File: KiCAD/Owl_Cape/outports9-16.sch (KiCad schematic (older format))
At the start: 33 parts, among them IC2 SN74LVC245AN, J10 G D V, J11 G D V, J12 G D V, J13 G D V, J14 G D V, J15 G D V, J16 G D V, J17 G D V

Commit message: updates to power components
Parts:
- renumbered J10 to J11, J11 to J12, J12 to J13, J13 to J14, J14 to J15, J15 to J16, J16 to J17, J17 to J18, R9 to R17, R10 to R18, R11 to R19, R12 to R20, R13 to R21, R14 to R22, R15 to R23, R16 to R24

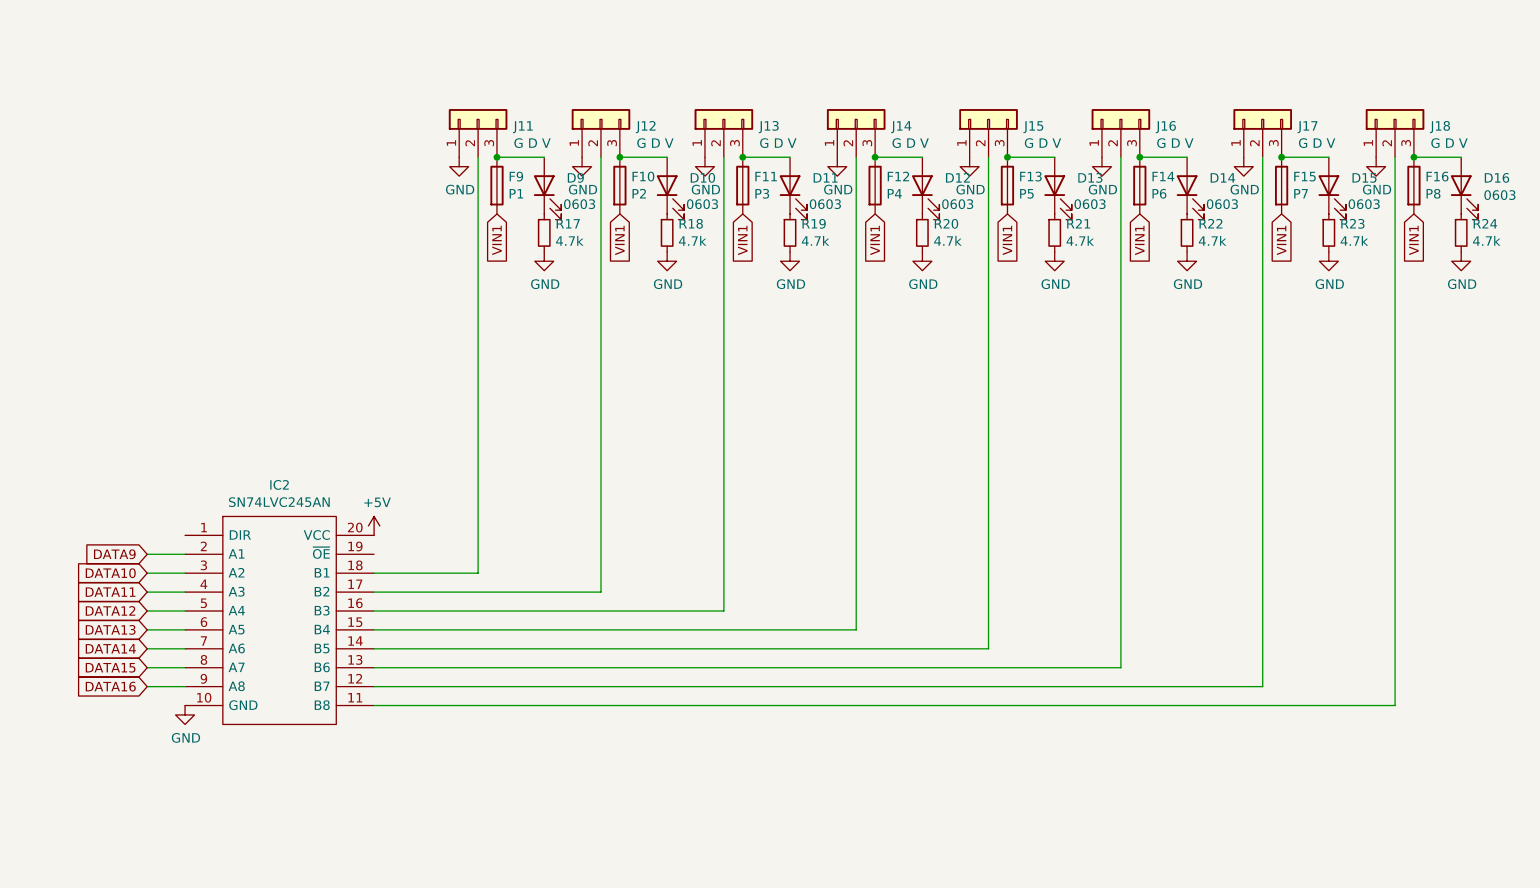
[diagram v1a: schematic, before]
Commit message: logo and kicad updates
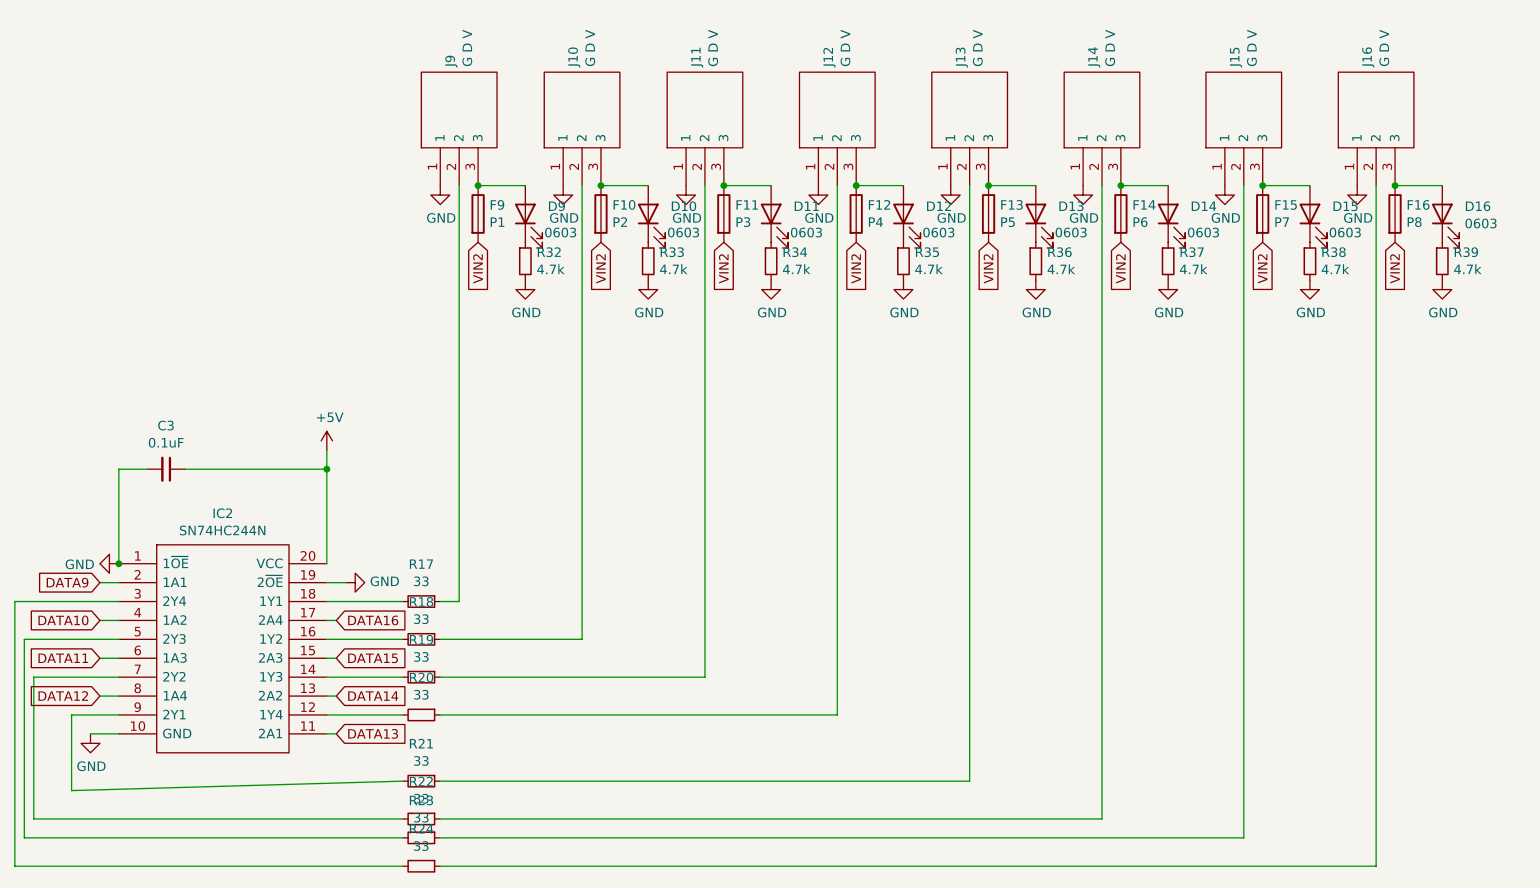
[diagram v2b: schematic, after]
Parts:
- removed IC2: SN74LVC245AN, SamacSys_Parts:DIP794W53P254L2540H508Q20N, symbol SamacSys_Parts:SN74LVC245AN
- removed J11, J12, J13, J14, J15, J16, J17, J18: G D V, PhoenixContact_MCV_1,5_3-G-3.5_1x03_P3.50mm_Vertical_Tim, symbol Connector_Generic:Conn_01x03
- added C3: 0.1uF, Capacitor_SMD:CP_Elec_4x5.3, symbol Device:C_Small
- added IC2: SN74HC244N, SamacSys_Parts:DIP794W53P254L2540H508Q20N, symbol SamacSys_Parts:SN74HC244N
- added J10, J11, J12, J13, J14, J15, J16, J9: G D V, SamacSys_Parts:SHDR3W80P0X350_1X3_1250X725X940P, symbol SamacSys_Parts:284514-3
- added R32, R33, R34, R35, R36, R37, R38, R39: 4.7k, Resistor_SMD:R_0805_2012Metric, symbol Device:R_Small
- D10, D11, D12, D13, D14, D15, D16, D9: footprint 3544again:LED_0603_1608Metric -> LED_SMD:LED_0603_1608Metric
- F10, F11, F12, F13, F14, F15, F16, F9: footprint 3544again:3544-2 -> Fuse:Fuseholder_Blade_Mini_Keystone_3568
- R17, R18, R19, R20, R21, R22, R23, R24: value 4.7k -> 33; footprint 3544again:R_0805_2012Metric -> Resistor_SMD:R_0805_2012Metric; Description C17673 -> (none)
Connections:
- net +5V: now also C3.1, IC2.20 (VCC)
- net DATA10: now also IC2.4 (1A2)
- net DATA11: now also IC2.6 (1A3)
- net DATA12: now also IC2.8 (1A4)
- net DATA13: now also IC2.11 (2A1)
- net DATA14: now also IC2.13 (2A2)
- net DATA15: now also IC2.15 (2A3)
- net DATA16: now also IC2.17 (2A4)
- net DATA9: now also IC2.2 (1A1)
- net GND: now also C3.2, IC2.1 (1~OE), IC2.10 (GND), IC2.19 (2~OE), J10.1, J11.1, J12.1, J13.1, J14.1, J15.1, J16.1, J9.1, R32.2, R33.2, R34.2, R35.2, R36.2, R37.2, R38.2, R39.2; no longer R17.2, R18.2, R19.2, R20.2, R21.2, R22.2, R23.2, R24.2
- net at D9.2 (A), F9.1: now also J9.3
- net at D10.2 (A), F10.1: now also J10.3
- net at D11.2 (A), F11.1: now also J11.3
- net at D12.2 (A), F12.1: now also J12.3
- net at D13.2 (A), F13.1: now also J13.3
- net at D14.2 (A), F14.1: now also J14.3
- net at D15.2 (A), F15.1: now also J15.3
- net at D16.2 (A), F16.1: now also J16.3
- net at D16.1 (K): now also R39.1; no longer R24.1
- net at D15.1 (K): now also R38.1; no longer R23.1
- net at D14.1 (K): now also R37.1; no longer R22.1
- net at D13.1 (K): now also R36.1; no longer R21.1
- net at D12.1 (K): now also R35.1; no longer R20.1
- net at D11.1 (K): now also R34.1; no longer R19.1
- net at D10.1 (K): now also R33.1; no longer R18.1
- net at D9.1 (K): now also R32.1; no longer R17.1
- net VIN1 renamed VIN2
- new net: J9.2, R17.1
- new net: IC2.12 (1Y4), R20.2
- new net: IC2.14 (1Y3), R19.2
- new net: IC2.16 (1Y2), R18.2
- new net: IC2.18 (1Y1), R17.2
- new net: IC2.3 (2Y4), R24.2
- new net: IC2.5 (2Y3), R23.2
- new net: IC2.7 (2Y2), R22.2
- new net: IC2.9 (2Y1), R21.2
- new net: J10.2, R18.1
- new net: J11.2, R19.1
- new net: J12.2, R20.1
- new net: J13.2, R21.1
- new net: J14.2, R22.1
- new net: J15.2, R23.1
- new net: J16.2, R24.1
